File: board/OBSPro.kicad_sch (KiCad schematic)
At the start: 0 parts

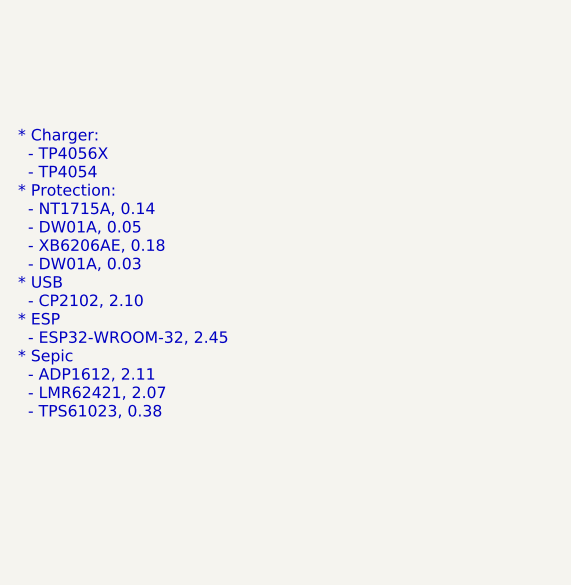
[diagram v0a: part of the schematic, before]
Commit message: New power management IC, some cleanup
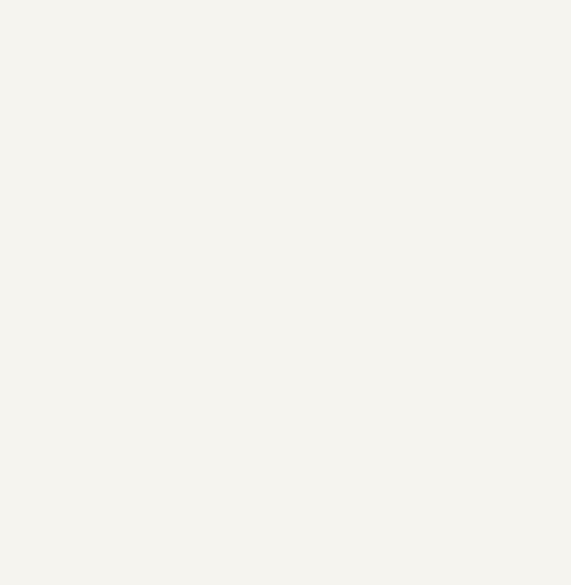
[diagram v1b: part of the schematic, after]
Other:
- note removed: "* Charger: - TP4056X - TP4054 * Protection: - NT1715A, 0.14 - DW01A, 0.05 - XB6206AE, 0.18 - DW01A, 0.03 * USB - CP2102, 2.10 * ESP - ESP32-WROOM-32, 2.45 * Sepic - ADP1612, 2.11 - LMR62421, 2.07 - TPS61023, 0.38"

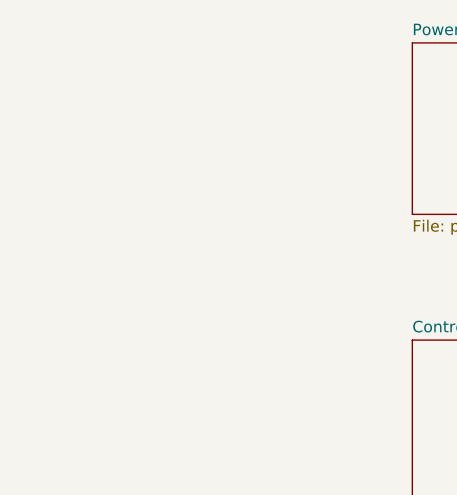
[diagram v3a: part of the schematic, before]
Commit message: First placement of parts, fixed a few bugs in the schematic
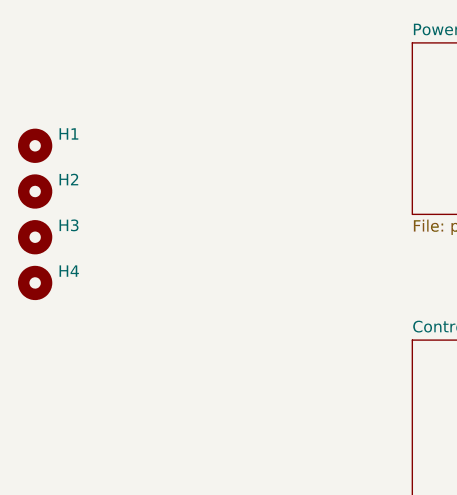
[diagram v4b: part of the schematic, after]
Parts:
- added H1, H2, H3, H4: MountingHole, MountingHole:MountingHole_3.2mm_M3, symbol Mechanical:MountingHole
